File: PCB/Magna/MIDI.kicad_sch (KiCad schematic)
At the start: 14 parts, among them J1001 DIN-5_180degree, J1002 DIN-5_180degree, J1003 DIN-5_180degree, U1001 6N137, U1002 74HC08D

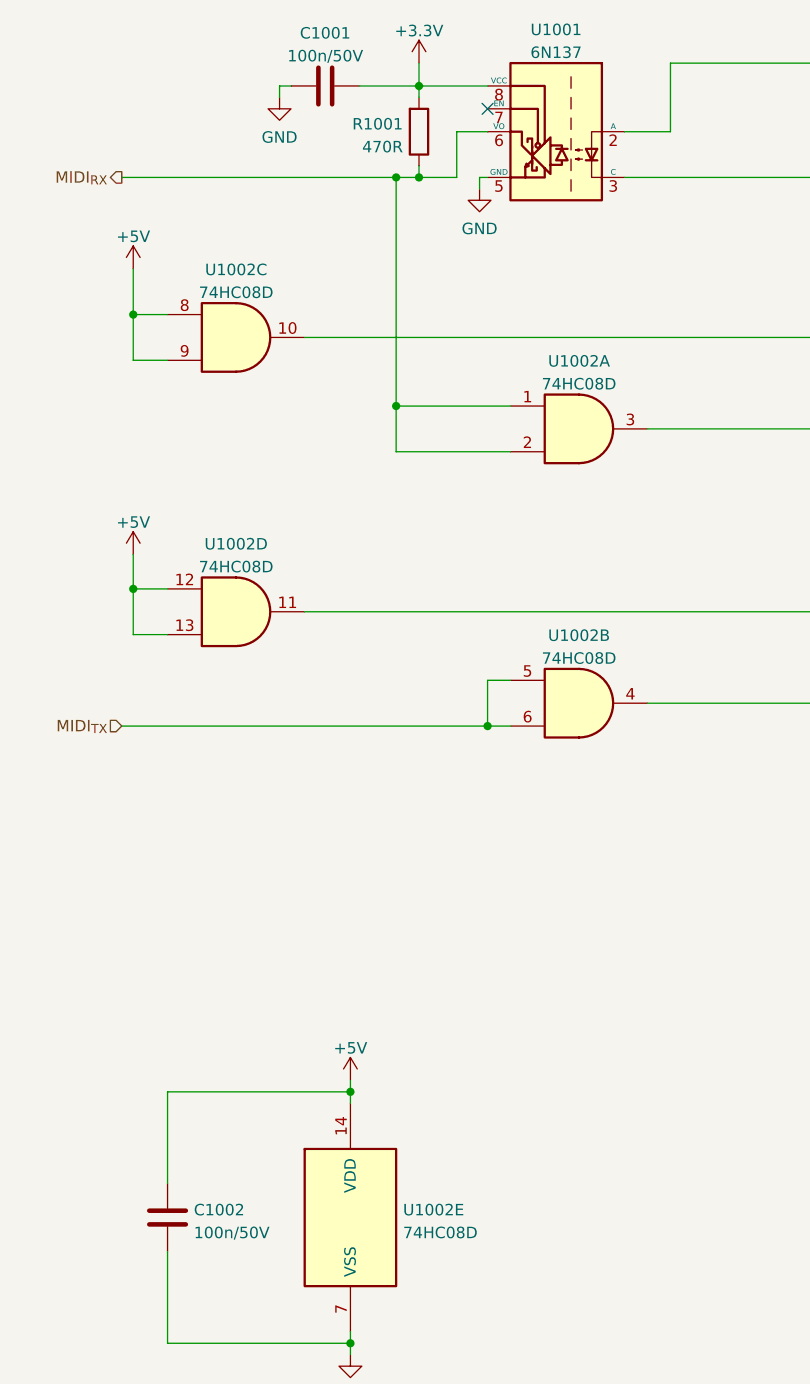
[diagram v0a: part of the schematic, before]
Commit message: Update analogue frontend and add potentiometer interface
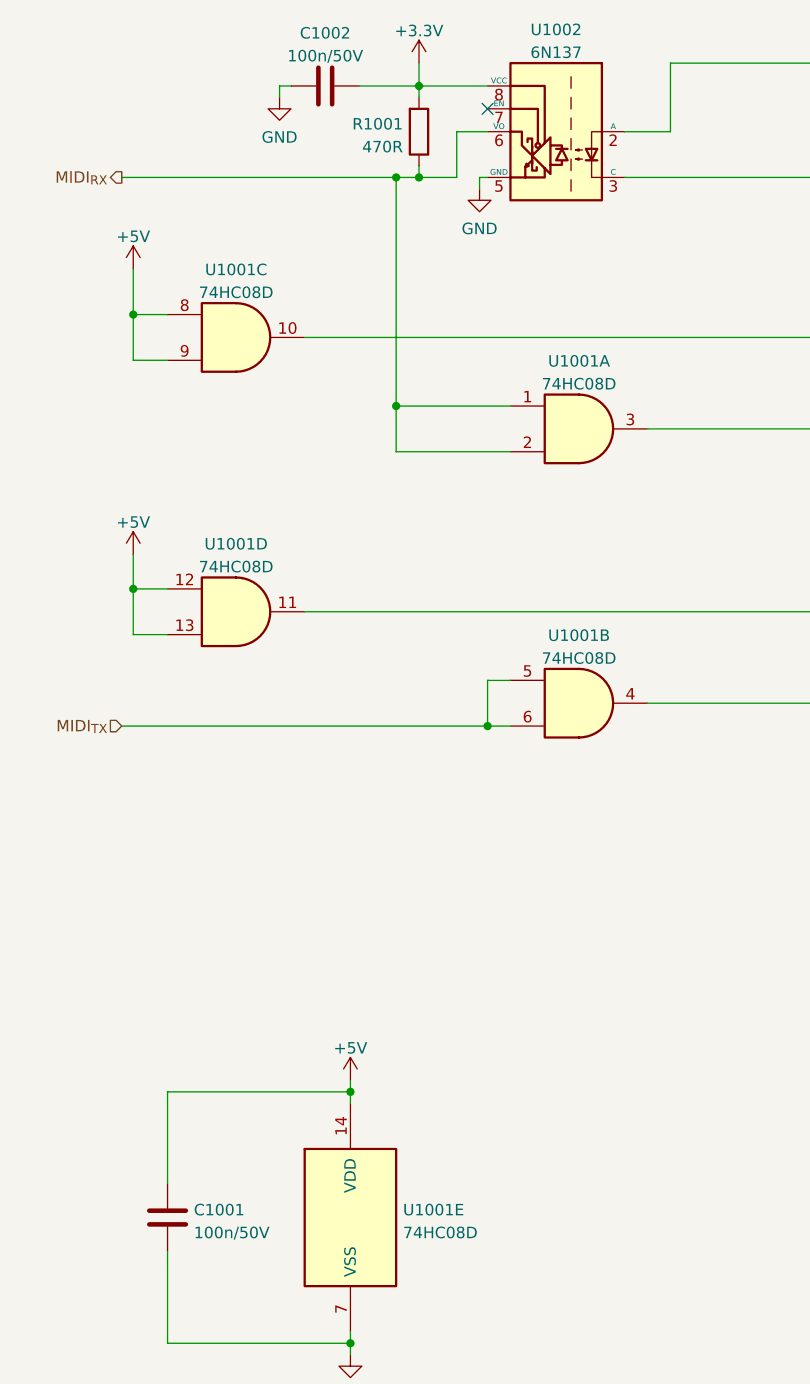
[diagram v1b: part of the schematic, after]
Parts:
- renumbered C1002 to C1001, C1001 to C1002, U1002 to U1001, U1001 to U1002

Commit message: Add final touched to all schematics
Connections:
- net +3.3V renamed VDD
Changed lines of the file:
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@@
   (junction (at 71.12 33.02) (diameter 0) (color 0 0 0 0)
   )
+  (junction (at 63.5 144.78) (diameter 0) (color 0 0 0 0)
+  )
   (junction (at 39.37 88.9) (diameter 0) (color 0 0 0 0)
   )
@@
   )
   (junction (at 39.37 58.42) (diameter 0) (color 0 0 0 0)
-  )
-  (junction (at 63.5 144.78) (diameter 0) (color 0 0 0 0)
   )
   (junction (at 68.58 43.18) (diameter 0) (color 0 0 0 0)
@@
   (no_connect (at 243.84 104.14))
   (no_connect (at 236.22 35.56))
-  (wire (pts (xy 77.851 43.18) (xy 77.851 44.45))
-    (stroke (width 0) (type default))
-  )
-  (wire (pts (xy 71.12 43.18) (xy 75.311 43.18))
+  (wire (pts (xy 78.74 43.18) (xy 78.74 45.72))
+    (stroke (width 0) (type default))
+  )
+  (wire (pts (xy 71.12 43.18) (xy 76.2 43.18))
     (stroke (width 0) (type default))
   )
@@
     (stroke (width 0) (type default))
   )
-  (wire (pts (xy 71.12 30.48) (xy 71.12 33.02))
-    (stroke (width 0) (type default))
-  )
-  (wire (pts (xy 75.311 38.1) (xy 78.74 38.1))
+  (wire (pts (xy 71.12 29.21) (xy 71.12 33.02))
+    (stroke (width 0) (type default))
+  )
+  (wire (pts (xy 76.2 38.1) (xy 78.74 38.1))
     (stroke (width 0) (type default))
   )
@@
     (stroke (width 0) (type default))
   )
-  (wire (pts (xy 55.626 33.02) (xy 55.626 34.29))
+  (wire (pts (xy 54.61 33.02) (xy 54.61 34.29))
     (stroke (width 0) (type default))
   )
@@
     (stroke (width 0) (type default))
   )
-  (wire (pts (xy 75.311 38.1) (xy 75.311 43.18))
+  (wire (pts (xy 76.2 38.1) (xy 76.2 43.18))
     (stroke (width 0) (type default))
   )
@@
     (stroke (width 0) (type default))
   )
-  (wire (pts (xy 77.851 43.18) (xy 78.74 43.18))
-    (stroke (width 0) (type default))
-  )
   (wire (pts (xy 78.74 104.14) (xy 78.74 99.06))
     (stroke (width 0) (type default))
@@
     (stroke (width 0) (type default))
   )
-  (wire (pts (xy 56.896 33.02) (xy 55.626 33.02))
+  (wire (pts (xy 57.15 33.02) (xy 54.61 33.02))
     (stroke (width 0) (type default))
   )
@@
     (stroke (width 0) (type default))
   )
+  (wire (pts (xy 63.5 144.78) (xy 63.5 146.05))
+    (stroke (width 0) (type default))
+  )
   (wire (pts (xy 38.1 43.18) (xy 68.58 43.18))
     (stroke (width 0) (type default))
@@
     (stroke (width 0) (type default))
   )
-  (wire (pts (xy 64.516 33.02) (xy 71.12 33.02))
+  (wire (pts (xy 64.77 33.02) (xy 71.12 33.02))
     (stroke (width 0) (type default))
   )
   (wire (pts (xy 99.06 38.1) (xy 93.98 38.1))
-    (stroke (width 0) (type default))
-  )
-  (wire (pts (xy 63.5 144.78) (xy 63.5 146.05))
     (stroke (width 0) (type default))
   )
@@
   (hierarchical_label "MIDI_{RX}" (shape output) (at 38.1 43.18 180) (fields_autoplaced)
     (effects (font (size 1.27 1.27)) (justify right))
+  )
+  (symbol (lib_id "power:VDD") (at 71.12 29.21 0) (unit 1)
+    (in_bom yes) (on_board yes) (dnp no) (fields_autoplaced)
+    (property "Reference" "#PWR01006" (at 71.12 33.02 0)
+      (effects (font (size 1.27 1.27)) hide)
+    )
+    (property "Value" "VDD" (at 71.12 24.13 0)
+      (effects (font (size 1.27 1.27)))
+    )
+    (property "Footprint" "" (at 71.12 29.21 0)
+      (effects (font (size 1.27 1.27)) hide)
+    )
+    (property "Datasheet" "" (at 71.12 29.21 0)
+      (effects (font (size 1.27 1.27)) hide)
+    )
+    (pin "1")
+    (instances
+      (project "Magna"
+        (path "/1469ea1f-a157-49dc-a369-2d42fa17695d/93ffa52a-dd6e-48b1-81f9-f219879f28f9"
+          (reference "#PWR01006") (unit 1)
+        )
+      )
+    )
   )
   (symbol (lib_id "Device:R") (at 196.85 91.44 90) (unit 1)
@@
     )
   )
-  (symbol (lib_id "power:GND") (at 55.626 34.29 0) (unit 1)
-    (in_bom yes) (on_board yes) (dnp no) (fields_autoplaced)
-    (property "Reference" "#PWR01003" (at 55.626 40.64 0)
-      (effects (font (size 1.27 1.27)) hide)
-    )
-    (property "Value" "GND" (at 55.626 38.7334 0)
-      (effects (font (size 1.27 1.27)))
-    )
-    (property "Footprint" "" (at 55.626 34.29 0)
-      (effects (font (size 1.27 1.27)) hide)
-    )
-    (property "Datasheet" "" (at 55.626 34.29 0)
+  (symbol (lib_id "power:GND") (at 54.61 34.29 0) (unit 1)
+    (in_bom yes) (on_board yes) (dnp no) (fields_autoplaced)
+    (property "Reference" "#PWR01003" (at 54.61 40.64 0)
+      (effects (font (size 1.27 1.27)) hide)
+    )
+    (property "Value" "GND" (at 54.61 38.7334 0)
+      (effects (font (size 1.27 1.27)))
+    )
+    (property "Footprint" "" (at 54.61 34.29 0)
+      (effects (font (size 1.27 1.27)) hide)
+    )
+    (property "Datasheet" "" (at 54.61 34.29 0)
       (effects (font (size 1.27 1.27)) hide)
     )
@@
     )
   )
-  (symbol (lib_id "Device:C") (at 60.706 33.02 90) (unit 1)
-    (in_bom yes) (on_board yes) (dnp no) (fields_autoplaced)
-    (property "Reference" "C1002" (at 60.706 27.1612 90)
-      (effects (font (size 1.27 1.27)))
-    )
-    (property "Value" "100n/50V" (at 60.706 29.6981 90)
-      (effects (font (size 1.27 1.27)))
-    )
-    (property "Footprint" "Capacitor_SMD:C_0603_1608Metric_Pad1.08x0.95mm_HandSolder" (at 64.516 32.0548 0)
-      (effects (font (size 1.27 1.27)) hide)
-    )
-    (property "Datasheet" "~" (at 60.706 33.02 0)
-      (effects (font (size 1.27 1.27)) hide)
-    )
-    (property "LCSC" "C14663" (at 60.706 33.02 0)
+  (symbol (lib_id "Device:C") (at 60.96 33.02 90) (unit 1)
+    (in_bom yes) (on_board yes) (dnp no) (fields_autoplaced)
+    (property "Reference" "C1002" (at 60.96 27.1612 90)
+      (effects (font (size 1.27 1.27)))
+    )
+    (property "Value" "100n/50V" (at 60.96 29.6981 90)
+      (effects (font (size 1.27 1.27)))
+    )
+    (property "Footprint" "Capacitor_SMD:C_0603_1608Metric_Pad1.08x0.95mm_HandSolder" (at 64.77 32.0548 0)
+      (effects (font (size 1.27 1.27)) hide)
+    )
+    (property "Datasheet" "~" (at 60.96 33.02 0)
+      (effects (font (size 1.27 1.27)) hide)
+    )
+    (property "LCSC" "C14663" (at 60.96 33.02 0)
       (effects (font (size 1.27 1.27)) hide)
     )
@@
       (effects (font (size 1.27 1.27)) hide)
     )
+    (property "Sim.Device" "D" (at 208.28 36.83 0)
+      (effects (font (size 1.27 1.27)) hide)
+    )
+    (property "Sim.Pins" "1=K 2=A" (at 208.28 36.83 0)
+      (effects (font (size 1.27 1.27)) hide)
+    )
     (pin "1")
     (pin "2")
@@
         (path "/f86ff50f-706c-4b52-a083-2f7e8e3afb1c/6a61af6a-88ef-4b64-8aa8-4a34e80ee921"
           (reference "#D?") (unit 1)
-        )
-      )
-    )
-  )
-  (symbol (lib_id "power:+3.3V") (at 71.12 30.48 0) (mirror y) (unit 1)
-    (in_bom yes) (on_board yes) (dnp no) (fields_autoplaced)
-    (property "Reference" "#PWR01006" (at 71.12 34.29 0)
-      (effects (font (size 1.27 1.27)) hide)
-    )
-    (property "Value" "+3.3V" (at 71.12 26.9042 0)
-      (effects (font (size 1.27 1.27)))
-    )
-    (property "Footprint" "" (at 71.12 30.48 0)
-      (effects (font (size 1.27 1.27)) hide)
-    )
-    (property "Datasheet" "" (at 71.12 30.48 0)
-      (effects (font (size 1.27 1.27)) hide)
-    )
-    (pin "1")
-    (instances
-      (project "Magna"
-        (path "/1469ea1f-a157-49dc-a369-2d42fa17695d/93ffa52a-dd6e-48b1-81f9-f219879f28f9"
-          (reference "#PWR01006") (unit 1)
-        )
-      )
-      (project "Ledwallcontroller"
-        (path "/f86ff50f-706c-4b52-a083-2f7e8e3afb1c/6a61af6a-88ef-4b64-8aa8-4a34e80ee921"
-          (reference "#PWR?") (unit 1)
         )
       )
@@
     )
   )
-  (symbol (lib_id "power:GND") (at 77.851 44.45 0) (unit 1)
-    (in_bom yes) (on_board yes) (dnp no) (fields_autoplaced)
-    (property "Reference" "#PWR01007" (at 77.851 50.8 0)
-      (effects (font (size 1.27 1.27)) hide)
-    )
-    (property "Value" "GND" (at 77.851 48.8934 0)
-      (effects (font (size 1.27 1.27)))
-    )
-    (property "Footprint" "" (at 77.851 44.45 0)
-      (effects (font (size 1.27 1.27)) hide)
-    )
-    (property "Datasheet" "" (at 77.851 44.45 0)
-      (effects (font (size 1.27 1.27)) hide)
-    )
+  (symbol (lib_id "power:GND") (at 78.74 45.72 0) (unit 1)
+    (in_bom yes) (on_board yes) (dnp no) (fields_autoplaced)
+    (property "Reference" "#PWR01007" (at 78.74 52.07 0)
+      (effects (font (size 1.27 1.27)) hide)
+    )
+    (property "Value" "GND" (at 78.74 50.1634 0)
+      (effects (font (size 1.27 1.27)))
+    )
+    (property "Footprint" "" (at 78.74 45.72 0)
+      (effects (font (size 1.27 1.27)) hide)
+    )
+    (property "Datasheet" "" (at 78.74 45.72 0)
+      (effects (font (size 1.27 1.27)) hide)
+    )

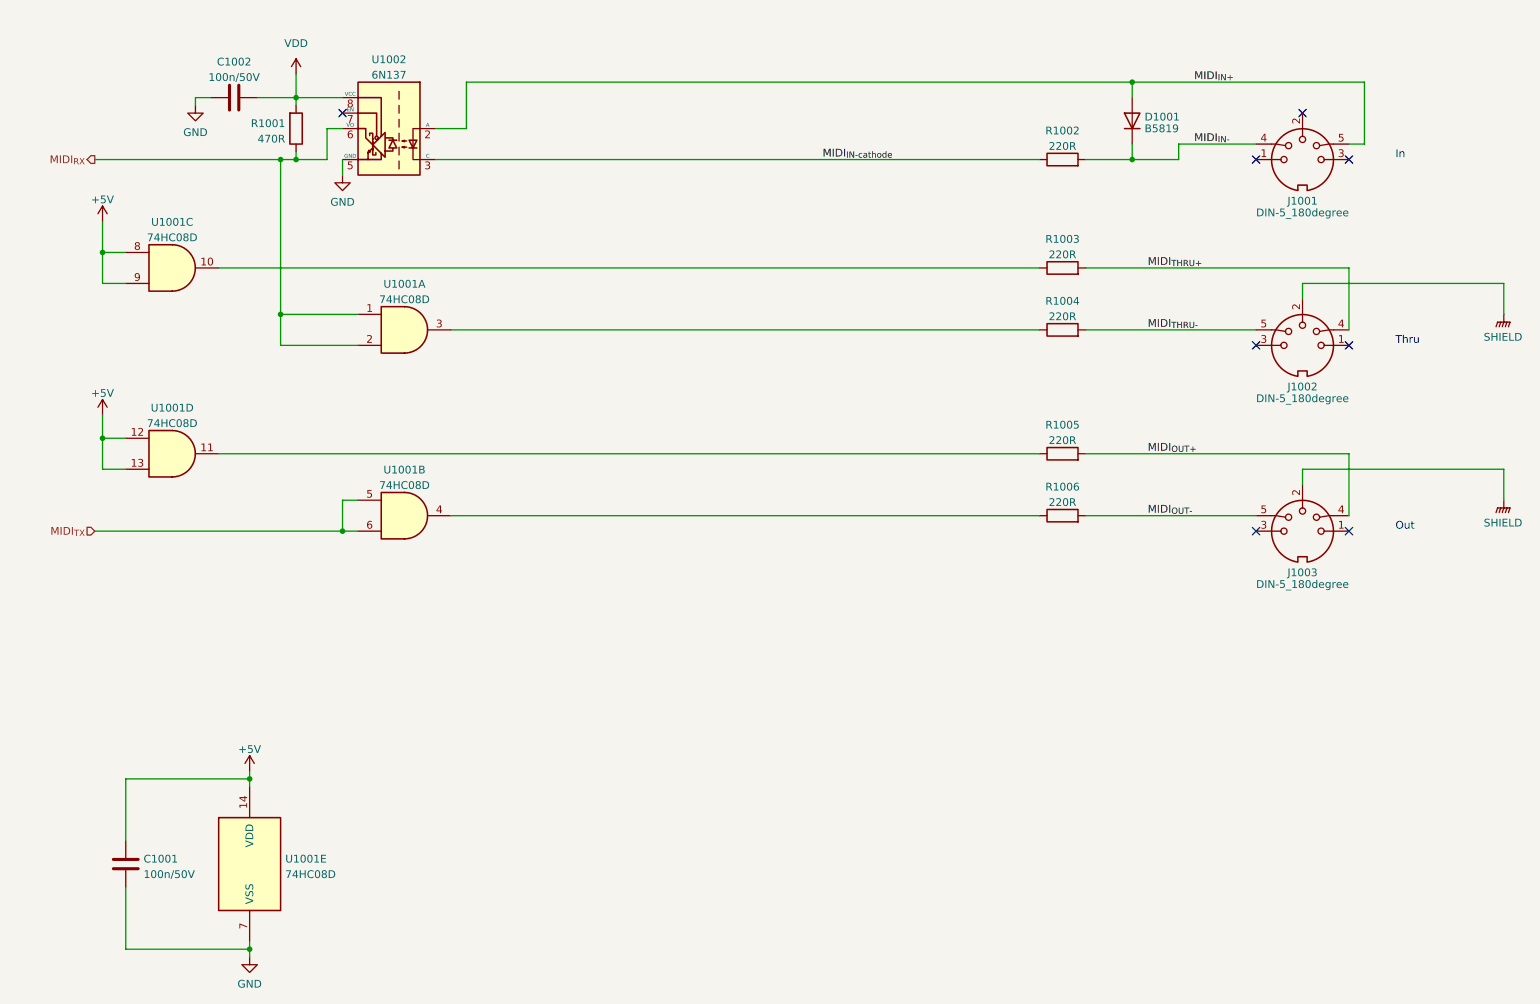
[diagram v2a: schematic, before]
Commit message: Remove all ERC in schematics
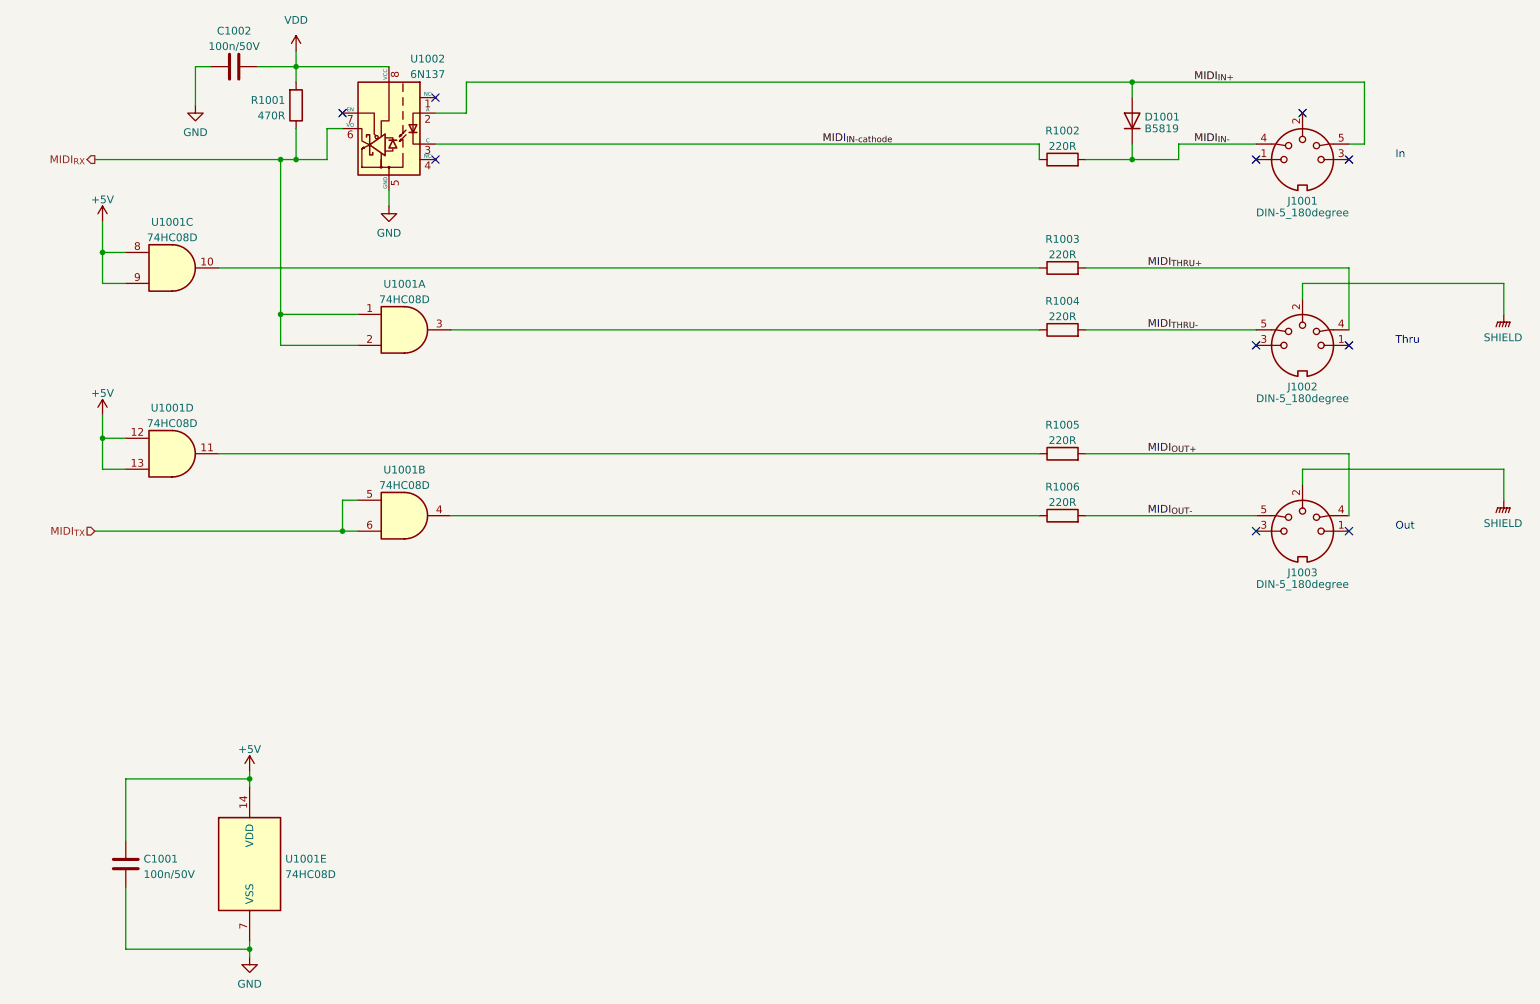
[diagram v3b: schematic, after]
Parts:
- U1002: footprint Package_SO:SSO-8_6.7x9.8mm_P2.54mm_Clearance8mm -> Package_DIP:DIP-8_W7.62mm
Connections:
- no-connect marks 8 -> 10
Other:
- moved on the sheet: C1002, R1001
